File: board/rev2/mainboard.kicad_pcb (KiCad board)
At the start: 4 copper layers, 161 parts, among them Q1 WSD40120DN56G, SW1 MS-22D28-G020, SW2 MS-22D28-G020, SW3 MS-22D28-G020, SW4 TS-1088-AR02016, SW5 MS-22D28-G020, U1 TPD6S300A, U10 74VHC161, U11 IS61LV256AL, U12 74AHCT595, U13 IS61LV256AL, U14 74AHCT595, U15 74HCT245, U16 74HCT245, U17 TS3USB30ERSWR, U18 TS3USB30ERSWR, U19 LD1117AG-33-AA3-A-R, U2 TPS62933, U3 TPS259472A, U4 LM5050-1, U5 SiC451, U6 STM32G071CBUx, U7 ESP32-C6-WROOM-1, U8 TLV74311, U9 RP2354B, Y1 ABM8-272-T3

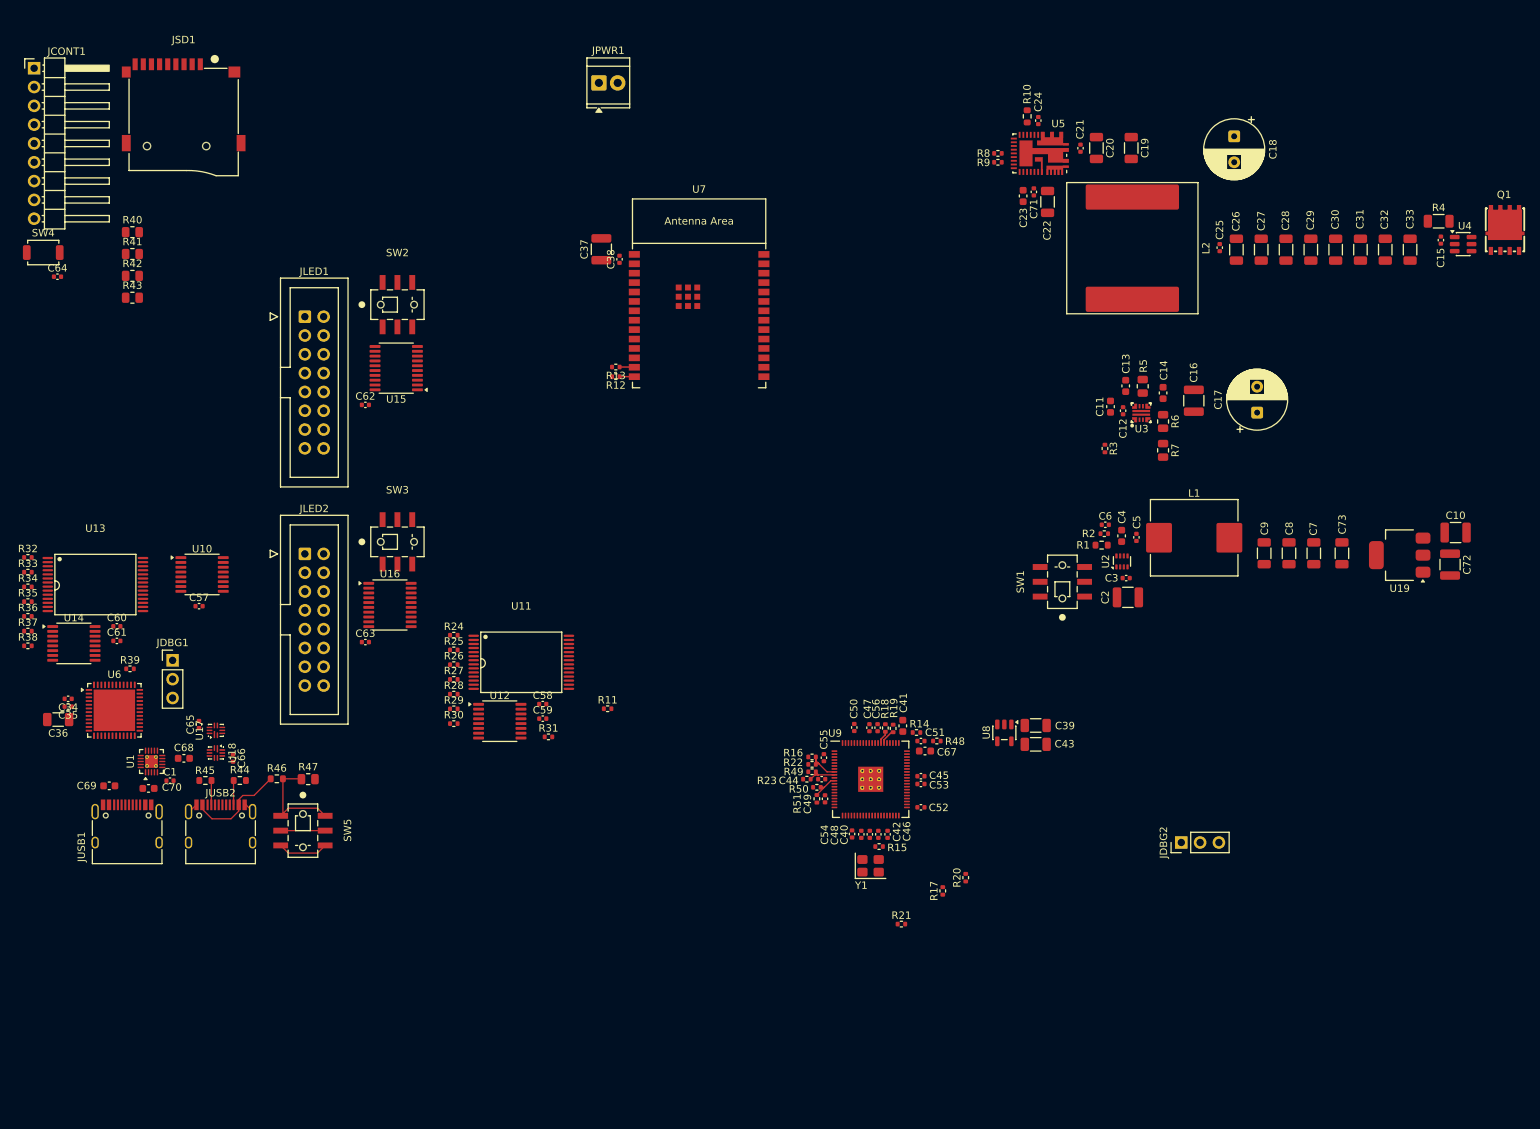
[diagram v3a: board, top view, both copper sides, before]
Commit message: Rough full board layout
also, start re-organizing which pins of buffers/gates are used for what

still need to reorder the mem i/o lines to align better

also fix duplicate pullups and fix mem_io isolation res
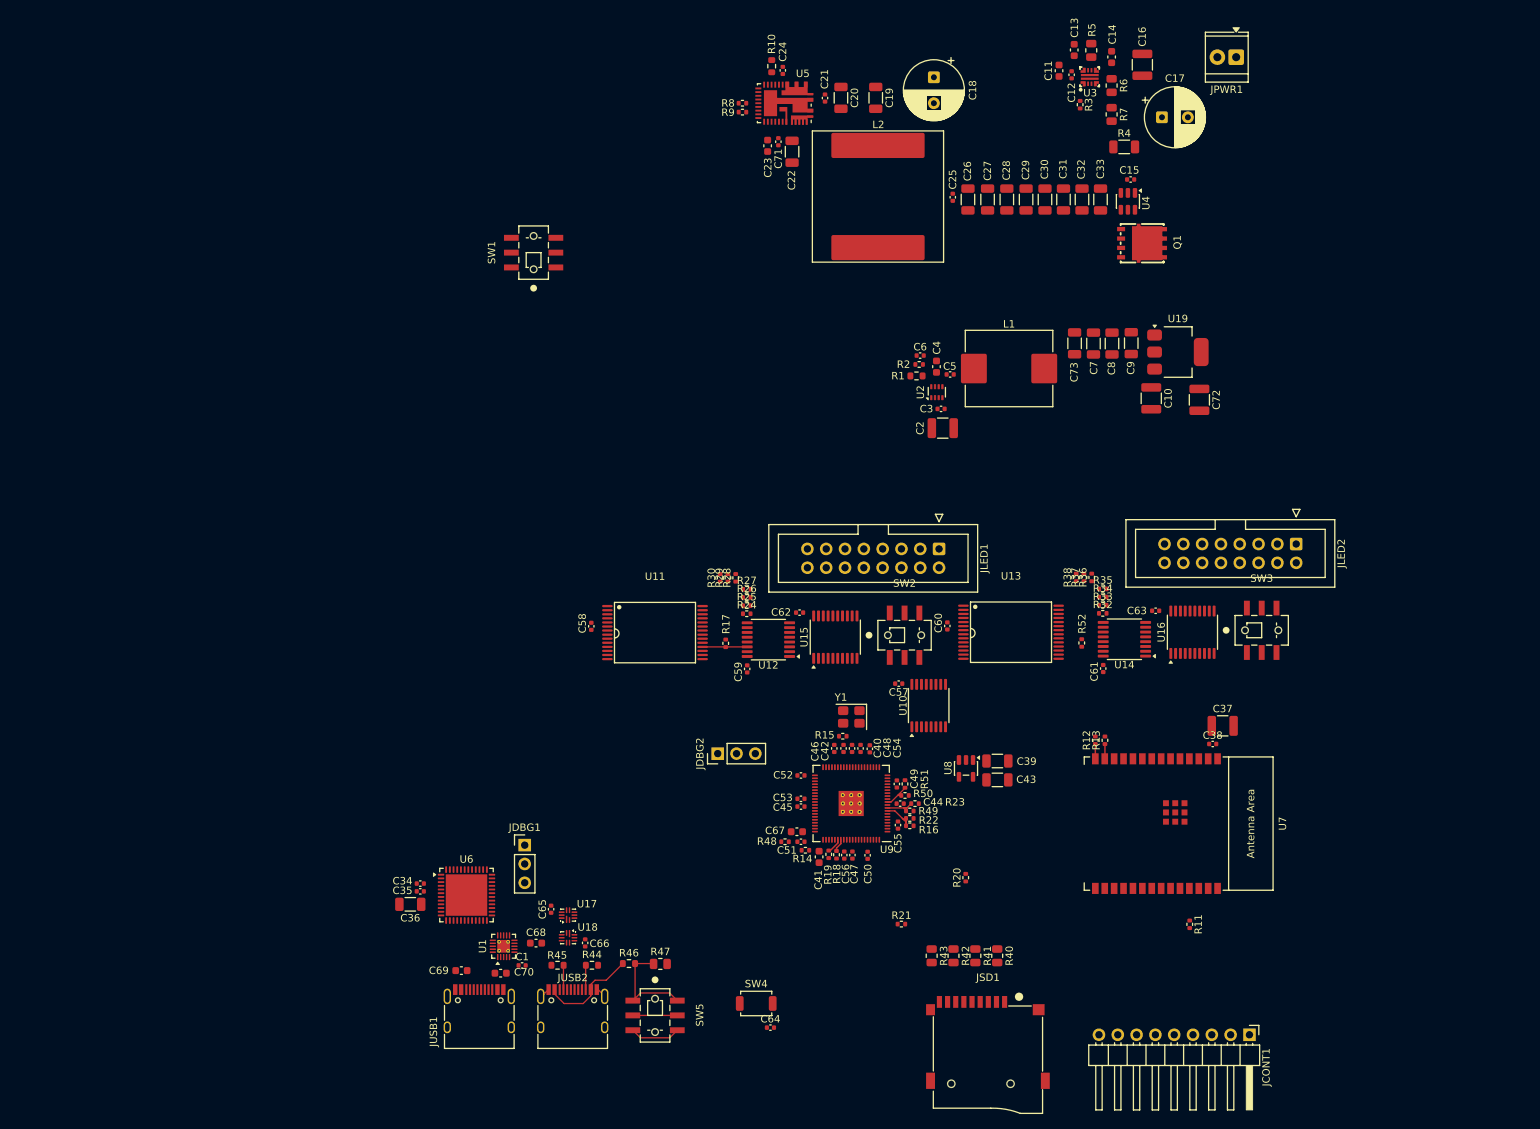
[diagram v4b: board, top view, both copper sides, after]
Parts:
- removed R31, R39: 10k, Resistor_SMD:R_0402_1005Metric
- added R52: 1k, Resistor_SMD:R_0402_1005Metric, F.Cu at (188.9, 107.3)
- moved JCONT1 209.7 mm to (211.5, 160.2), turned to -90 degrees
- moved JSD1 166.8 mm to (176.2, 161.0)
- moved R40 152.3 mm to (177.4, 149.5), turned to -90 degrees
- moved R41 148.1 mm to (174.5, 149.5), turned to -90 degrees
- moved R32 145.3 mm to (191.7, 103.3)
- moved R33 145.2 mm to (191.7, 102.2)
- moved R35 145.2 mm to (191.7, 100.0)
- moved R34 145.1 mm to (191.7, 101.1)
- moved R42 144.0 mm to (171.6, 149.5), turned to -90 degrees
- moved R36 143.7 mm to (190.2, 98.4), turned to 90 degrees
- moved R37 142.8 mm to (189.2, 98.4), turned to 90 degrees
- moved U14 141.9 mm to (194.6, 106.8), turned to 180 degrees
- moved R38 141.9 mm to (188.1, 98.4), turned to 90 degrees
- moved SW4 139.8 mm to (144.9, 155.9)
- moved C64 139.8 mm to (146.8, 159.2)
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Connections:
- JLED1 pad 10: /LED Connection A/PANEL.LAT -> /LED Connection A/PANEL.B
- JLED1 pad 11: /LED Connection A/PANEL.D -> /LED Connection A/PANEL.C
- JLED1 pad 12: /LED Connection A/PANEL.B -> /LED Connection A/PANEL.D
- JLED1 pad 13: Net-(JLED1-Pin_13) -> /LED Connection A/PANEL.CLK
- JLED1 pad 14: /Decoder/PANELA.G1 -> /LED Connection A/PANEL.LAT
- JLED1 pad 15: Net-(JLED1-Pin_15) -> /LED Connection A/PANEL.OE
- JLED1 pad 16: /Decoder/PANELA.G0 -> GND
- JLED1 pad 2: /Decoder/PANELA.B0 -> /Decoder/PANELA.G0
- JLED1 pad 3: /Decoder/PANELA.R1 -> /Decoder/PANELA.B0
- JLED1 pad 4: /Decoder/PANELA.B1 -> Net-(JLED1-Pin_4)
- JLED1 pad 5: /LED Connection A/PANEL.A -> /Decoder/PANELA.R1
- JLED1 pad 6: /LED Connection A/PANEL.C -> /Decoder/PANELA.G1
- JLED1 pad 7: /LED Connection A/PANEL.CLK -> /Decoder/PANELA.B1
- JLED1 pad 8: /LED Connection A/PANEL.OE -> Net-(JLED1-Pin_8)
- JLED1 pad 9: GND -> /LED Connection A/PANEL.A
- JLED2 pad 10: /LED Connection B/PANEL.LAT -> /LED Connection B/PANEL.B
- JLED2 pad 11: /LED Connection B/PANEL.D -> /LED Connection B/PANEL.C
- JLED2 pad 12: /LED Connection B/PANEL.B -> /LED Connection B/PANEL.D
- JLED2 pad 13: Net-(JLED2-Pin_13) -> /LED Connection B/PANEL.CLK
- JLED2 pad 14: /Decoder/PANELB.G1 -> /LED Connection B/PANEL.LAT
- JLED2 pad 15: Net-(JLED2-Pin_15) -> /LED Connection B/PANEL.OE
- JLED2 pad 16: /Decoder/PANELB.G0 -> GND
- JLED2 pad 2: /Decoder/PANELB.B0 -> /Decoder/PANELB.G0
- JLED2 pad 3: /Decoder/PANELB.R1 -> /Decoder/PANELB.B0
- JLED2 pad 4: /Decoder/PANELB.B1 -> Net-(JLED2-Pin_4)
- JLED2 pad 5: /LED Connection B/PANEL.A -> /Decoder/PANELB.R1
- JLED2 pad 6: /LED Connection B/PANEL.C -> /Decoder/PANELB.G1
- JLED2 pad 7: /LED Connection B/PANEL.CLK -> /Decoder/PANELB.B1
- JLED2 pad 8: /LED Connection B/PANEL.OE -> Net-(JLED2-Pin_8)
- JLED2 pad 9: GND -> /LED Connection B/PANEL.A
- R17 pad 1: Net-(U9-GPIO47_ADC7) -> Net-(U11-I/O0)
- SW2 pad 2: Net-(JLED1-Pin_15) -> Net-(JLED1-Pin_4)
- SW2 pad 5: Net-(JLED1-Pin_13) -> Net-(JLED1-Pin_8)
- SW3 pad 2: Net-(JLED2-Pin_15) -> Net-(JLED2-Pin_4)
- SW3 pad 5: Net-(JLED2-Pin_13) -> Net-(JLED2-Pin_8)
- U11 pad 10: /Decoder/PIX_MEM_PB0 -> /Decoder/PIX_MEM_PA0
- U11 pad 11: /Decoder/MEM_IO -> Net-(U11-I/O0)
- U11 pad 3: /Decoder/PIX_MEM_PB7 -> /Decoder/PIX_MEM_PA7
- U11 pad 4: /Decoder/PIX_MEM_PB6 -> /Decoder/PIX_MEM_PA6
- U11 pad 5: /Decoder/PIX_MEM_PB5 -> /Decoder/PIX_MEM_PA5
- U11 pad 6: /Decoder/PIX_MEM_PB4 -> /Decoder/PIX_MEM_PA4
- U11 pad 7: /Decoder/PIX_MEM_PB3 -> /Decoder/PIX_MEM_PA3
- U11 pad 8: /Decoder/PIX_MEM_PB2 -> /Decoder/PIX_MEM_PA2
- U11 pad 9: /Decoder/PIX_MEM_PB1 -> /Decoder/PIX_MEM_PA1
- U12 pad 14: /Decoder/MEM_IO -> Net-(U11-I/O0)
- U13 pad 10: /Decoder/PIX_MEM_PA0 -> /Decoder/PIX_MEM_PB0
- U13 pad 11: /Decoder/MEM_IO -> Net-(U13-I/O0)
- U13 pad 3: /Decoder/PIX_MEM_PA7 -> /Decoder/PIX_MEM_PB7
- U13 pad 4: /Decoder/PIX_MEM_PA6 -> /Decoder/PIX_MEM_PB6
- U13 pad 5: /Decoder/PIX_MEM_PA5 -> /Decoder/PIX_MEM_PB5
- U13 pad 6: /Decoder/PIX_MEM_PA4 -> /Decoder/PIX_MEM_PB4
- U13 pad 7: /Decoder/PIX_MEM_PA3 -> /Decoder/PIX_MEM_PB3
- U13 pad 8: /Decoder/PIX_MEM_PA2 -> /Decoder/PIX_MEM_PB2
- U13 pad 9: /Decoder/PIX_MEM_PA1 -> /Decoder/PIX_MEM_PB1
- U14 pad 14: /Decoder/MEM_IO -> Net-(U13-I/O0)
- U15 pad 11: /LED Connection A/PANEL.LAT -> /LED Connection A/PANEL.E
- U15 pad 12: /LED Connection A/PANEL.OE -> /LED Connection A/PANEL.A
- U15 pad 13: /LED Connection A/PANEL.CLK -> /LED Connection A/PANEL.B
- U15 pad 14: /LED Connection A/PANEL.E -> /LED Connection A/PANEL.C
- U15 pad 16: /LED Connection A/PANEL.C -> /LED Connection A/PANEL.LAT
- U15 pad 17: /LED Connection A/PANEL.B -> /LED Connection A/PANEL.CLK
- U15 pad 18: /LED Connection A/PANEL.A -> /LED Connection A/PANEL.OE
- U15 pad 2: /Display MCU/RMUX_A -> /Display MCU/PANEL_LAT
- U15 pad 3: /Display MCU/RMUX_B -> /Display MCU/~{PIX_CLK}
- U15 pad 4: /Display MCU/RMUX_C -> /Display MCU/PANEL_OE
- U15 pad 6: /Display MCU/RMUX_E -> /Display MCU/RMUX_C
- U15 pad 7: /Display MCU/~{PIX_CLK} -> /Display MCU/RMUX_B
- U15 pad 8: /Display MCU/PANEL_OE -> /Display MCU/RMUX_A
- U15 pad 9: /Display MCU/PANEL_LAT -> /Display MCU/RMUX_E
- U16 pad 11: /LED Connection B/PANEL.LAT -> /LED Connection B/PANEL.E
- U16 pad 12: /LED Connection B/PANEL.OE -> /LED Connection B/PANEL.A
- U16 pad 13: /LED Connection B/PANEL.CLK -> /LED Connection B/PANEL.B
- U16 pad 14: /LED Connection B/PANEL.E -> /LED Connection B/PANEL.C
- U16 pad 16: /LED Connection B/PANEL.C -> /LED Connection B/PANEL.LAT
- U16 pad 17: /LED Connection B/PANEL.B -> /LED Connection B/PANEL.CLK
- U16 pad 18: /LED Connection B/PANEL.A -> /LED Connection B/PANEL.OE
- U16 pad 2: /Display MCU/RMUX_A -> /Display MCU/PANEL_LAT
- U16 pad 3: /Display MCU/RMUX_B -> /Display MCU/~{PIX_CLK}
- U16 pad 4: /Display MCU/RMUX_C -> /Display MCU/PANEL_OE
- U16 pad 6: /Display MCU/RMUX_E -> /Display MCU/RMUX_C
- U16 pad 7: /Display MCU/~{PIX_CLK} -> /Display MCU/RMUX_B
- U16 pad 8: /Display MCU/PANEL_OE -> /Display MCU/RMUX_A
- U16 pad 9: /Display MCU/PANEL_LAT -> /Display MCU/RMUX_E
- U9 pad 58: Net-(U9-GPIO47_ADC7) -> /Decoder/MEM_IO
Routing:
- net Net-(U11-I/O0): track 0.00 -> 6.02 mm

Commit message: Start routing rev2 board
- got component placement mostly done, board outline set
- did the power planes for the regulators, still need to do thermal
  relief stuff and setup the board-global power planes
- then the big thing is the high freq stuff, then its just connect the
  dots hopefully
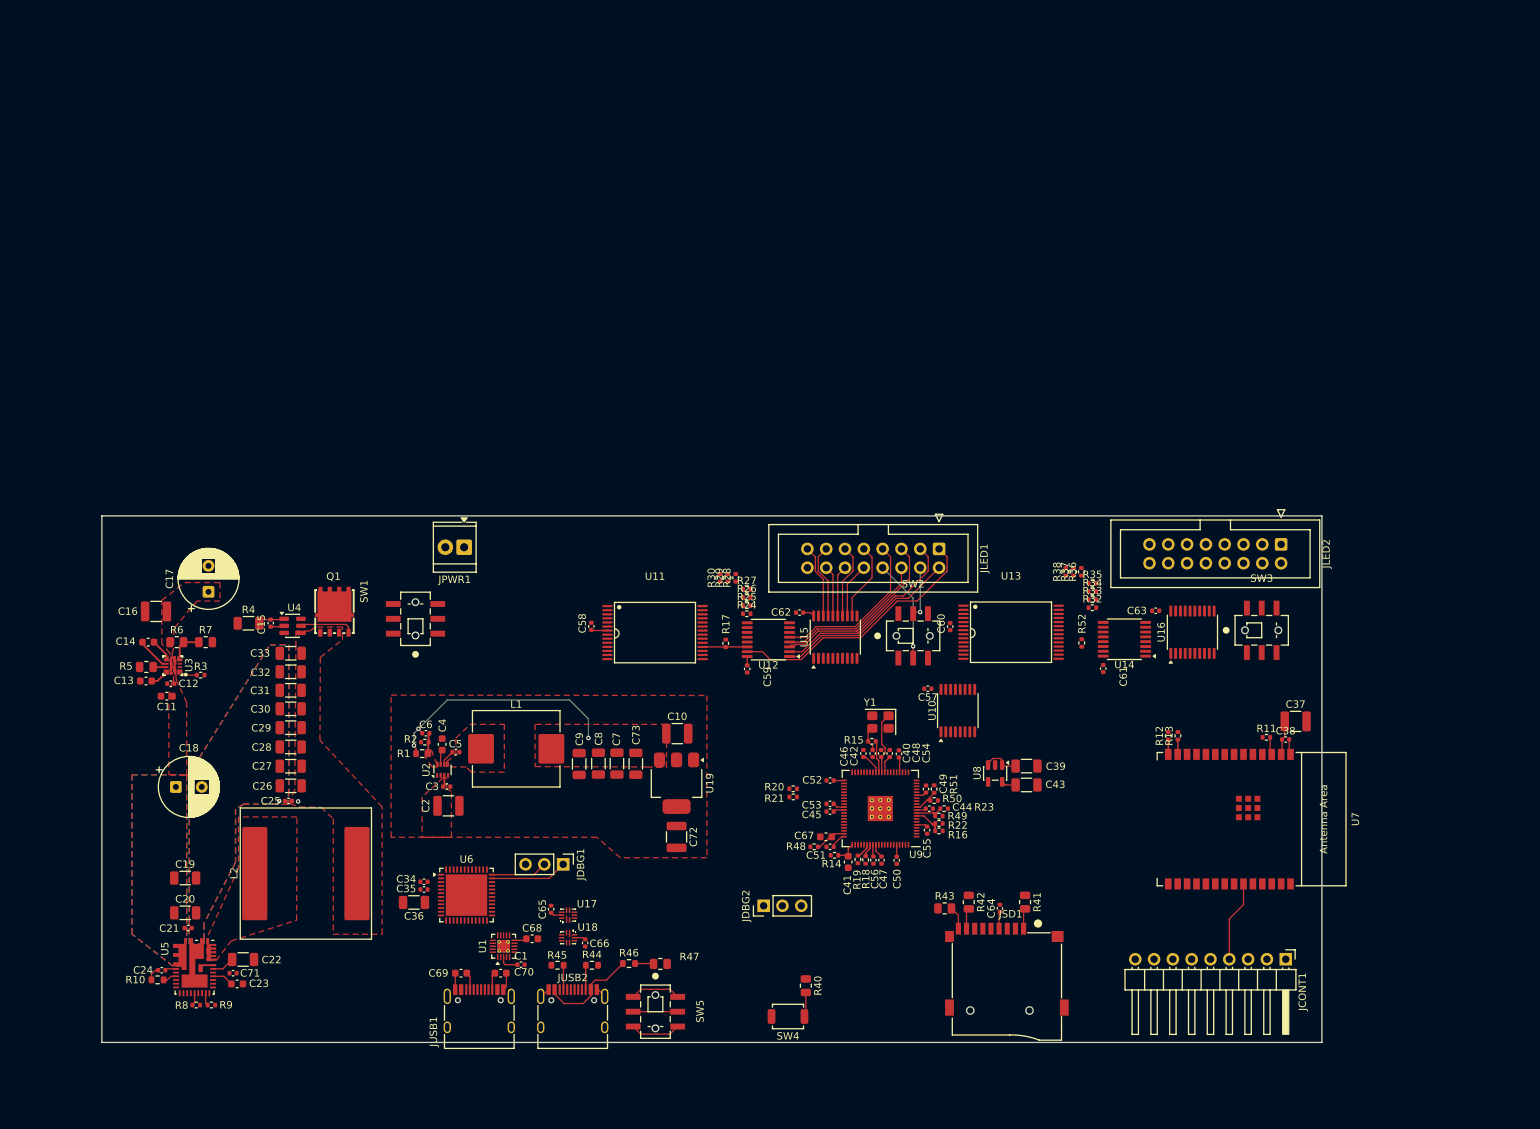
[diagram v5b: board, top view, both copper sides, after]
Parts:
- moved R5 152.4 mm to (62.6, 110.5), turned to 180 degrees
- moved C16 152.3 mm to (63.9, 103.0), turned to 180 degrees
- moved C14 152.2 mm to (62.8, 107.2), turned to 180 degrees
- moved C13 151.6 mm to (62.5, 112.4), turned to 180 degrees
- moved R10 148.7 mm to (64.1, 152.8), turned to 0 degrees
- moved C24 147.6 mm to (64.6, 151.4), turned to 180 degrees
- moved C11 147.1 mm to (65.3, 114.5), turned to 180 degrees
- moved U3 147.1 mm to (66.2, 110.3), turned to 180 degrees
- moved R6 146.9 mm to (66.7, 107.2), turned to 0 degrees
- moved C12 146.8 mm to (65.9, 112.8), turned to 180 degrees
- moved C17 143.8 mm to (71.0, 100.4), turned to 90 degrees
- moved R8 142.4 mm to (69.3, 156.2), turned to 0 degrees
- moved R7 141.6 mm to (70.6, 107.2), turned to 0 degrees
- moved R3 141.5 mm to (69.9, 111.6), turned to 0 degrees
- moved C21 141.3 mm to (68.2, 145.8), turned to 0 degrees
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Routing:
- net VDD: track 0.00 -> 36.8 mm
- net /Decoder/PANELA.R0: track 0.00 -> 35.8 mm
- net Net-(U19-VI): track 0.00 -> 32.7 mm, vias 0 -> 3
- net /Decoder/PANELA.B0: track 0.00 -> 26.7 mm
- net /Decoder/PANELA.G0: track 0.00 -> 25.1 mm
- net /Decoder/PANELA.R1: track 0.00 -> 24.5 mm
- net /Decoder/PANELA.B1: track 0.00 -> 22.4 mm
- net /Decoder/PANELA.G1: track 0.00 -> 20.5 mm
- net Net-(JLED1-Pin_8): track 0.00 -> 13.9 mm, vias 0 -> 1
- net GND: track 9.75 -> 22.9 mm
- net /Peripherals/MENBTN: track 0.00 -> 11.0 mm
- net /LED Connection A/PANEL.A: track 0.00 -> 10.6 mm
- net Net-(JDBG1-Pin_1): track 0.00 -> 10.4 mm
- net /LED Connection A/PANEL.C: track 0.00 -> 10.1 mm
- net /LED Connection A/PANEL.CLK: track 0.00 -> 10.0 mm
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- added copper zone on F.Cu, net +5V
- added copper zone on F.Cu, net /Power/5V_REG
- added copper zone on B.Cu, net /Power/VBUS
- added copper zone on F.Cu, net /Power/VBUS
- added copper zone on B.Cu, net GND
- added copper zone on F.Cu, net GND
- added copper zone on F.Cu, net Net-(U19-VI)
- added copper zone on F.Cu, net Net-(U2-FB)
- added copper zone on F.Cu, net Net-(U2-SW)
- added copper zone on F.Cu, net Net-(U2-VIN)
- added copper zone on F.Cu, net Net-(U5-SW)
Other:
- board outline added: 164.8 x 71.1 mm
